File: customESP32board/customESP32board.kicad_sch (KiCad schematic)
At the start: 46 parts, among them J1 USB_B_Micro, J2 Conn_01x16_Pin, J3 Conn_01x16_Pin, Q1 S8050, Q2 S8050, Q3 BSS138, Q4 BSS138, Q5 BSS138, SW1 SW_Push, SW2 SW_Push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

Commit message: assigned footprint to all symbols
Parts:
- C1, C7: footprint (none) -> Capacitor_SMD:C_0805_2012Metric; link (none) -> https://makerselectronics.com/product/multilayer-ceramic-ca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
- C11: footprint (none) -> Capacitor_SMD:C_1206_3216Metric; link (none) -> https://uge-one.com/product/1206-solid-tantalum-smd-chip-ca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
- C3, C6: footprint (none) -> Capacitor_SMD:C_0603_1608Metric; link (none) -> https://makerselectronics.com/product/multilayer-ceramic-sm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
- D1: footprint Diode_THT:D_DO-41_SOD81_P10.16mm_Horizontal -> Diode_SMD:D_SMA_Handsoldering
- D11, D6, D7, D8: footprint (none) -> LED_THT:LED_D5.0mm-4_RGB
- D5, D9: footprint (none) -> LED_SMD:LED_0603_1608Metric
- J1: footprint (none) -> Connector_USB:USB_Micro-B_Wuerth_629105150521
- J2, J3: footprint (none) -> Connector_PinHeader_2.54mm:PinHeader_1x16_P2.54mm_Vertical; link (none) -> https://uge-one.com/product/pin-header-female-1x16-straight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
- R1, R11, R12, R16, R17, R18, R2, R3: footprint (none) -> Resistor_SMD:R_0805_2012Metric
- R10, R13, R14, R15, R4, R7, R8, R9: footprint (none) -> Resistor_SMD:R_0603_1608Metric
- R5, R6: footprint (none) -> Resistor_SMD:R_1206_3216Metric
- SW1: footprint (none) -> TS-1088-AR02016:SW_TS-1088-AR02016
- SW2: footprint (none) -> TS-1088-AR02016:SW_TS-1088-AR02016; link https://uge-one.com/product/smd-micro-push-button-switch-2p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 -> https://uge-one.com/product/smd-micro-switch-white-tact-s-3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
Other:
- title: customESP32S by Eng/Ahmed Adel -> customESP32board by Eng/Ahmed Adel
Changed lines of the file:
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@@
 	(paper "A4")
 	(title_block
-		(title "customESP32S by Eng/Ahmed Adel")
+		(title "customESP32board by Eng/Ahmed Adel")
 		(date "2025-09-23")
 		(rev "V1_1")
@@
 			)
 		)
-		(property "Footprint" ""
+		(property "Footprint" "Resistor_SMD:R_0603_1608Metric"
 			(at 140.97 120.142 90)
 			(effects
@@
 			)
 		)
-		(property "Footprint" ""
+		(property "Footprint" "LED_THT:LED_D5.0mm-4_RGB"
 			(at 201.93 90.17 0)
 			(effects
@@
 			)
 		)
-		(property "Footprint" ""
+		(property "Footprint" "Resistor_SMD:R_0805_2012Metric"
 			(at 190.5 141.478 90)
 			(effects
@@
 			)
 		)
-		(property "Footprint" ""
+		(property "Footprint" "Resistor_SMD:R_0603_1608Metric"
 			(at 147.32 64.008 90)
 			(effects
@@
 			)
 		)
-		(property "Footprint" ""
+		(property "Footprint" "Resistor_SMD:R_0805_2012Metric"
 			(at 145.542 127 90)
 			(effects
@@
 			)
 		)
-		(property "Footprint" ""
+		(property "Footprint" "Capacitor_SMD:C_1206_3216Metric"
 			(at 59.3852 95.25 0)
 			(effects
@@
 			)
 		)
-		(property "link" ""
+		(property "link" "https://uge-one.com/product/1206-solid-tantalum-smd-chip-capacitors-22uf-10v-type-a-3216/?srsltid=AfmBOopTQ543hj2REw3LW1Aad3g4Vye15Z8vCZf5dY69xXFxijASt_x6"
 			(at 58.42 91.44 0)
 			(effects
@@
 			)
 		)
-		(property "Footprint" ""
+		(property "Footprint" "Resistor_SMD:R_1206_3216Metric"
 			(at 107.188 38.1 90)
 			(effects
@@
 			)
 		)
-		(property "Footprint" ""
+		(property "Footprint" "Resistor_SMD:R_0805_2012Metric"
 			(at 190.5 151.638 90)
 			(effects
@@
 			)
 		)
-		(property "Footprint" ""
+		(property "Footprint" "Resistor_SMD:R_0805_2012Metric"
 			(at 145.542 165.1 90)
 			(effects
@@
 			)
 		)
-		(property "Footprint" ""
+		(property "Footprint" "Resistor_SMD:R_1206_3216Metric"
 			(at 93.218 38.1 90)
 			(effects
@@
 			)
 		)
-		(property "Footprint" ""
+		(property "Footprint" "Resistor_SMD:R_0805_2012Metric"
 			(at 87.63 151.638 90)
 			(effects
@@
 			)
 		)
-		(property "Footprint" ""
+		(property "Footprint" "Connector_USB:USB_Micro-B_Wuerth_629105150521"
 			(at 25.4 41.91 0)
 			(effects
@@
 			)
 		)
-		(property "Footprint" ""
+		(property "Footprint" "Connector_PinHeader_2.54mm:PinHeader_1x16_P2.54mm_Vertical"
 			(at 248.92 134.62 0)
 			(effects
@@
 			)
 		)
-		(property "Datasheet" "~"
+		(property "Datasheet" "https://uge-one.com/product/pin-header-female-1x16-straight-connector-2-54mm-pitch-blue/?srsltid=AfmBOoow7MnGPupESH2Bn80hXHz93AXS_C1RnlKSbnqCmVDw4ILT8D4U"
 			(at 248.92 134.62 0)
 			(effects
@@
 			)
 		)
-		(property "link" ""
+		(property "link" "https://uge-one.com/product/pin-header-female-1x16-straight-connector-2-54mm-pitch-blue/?srsltid=AfmBOoow7MnGPupESH2Bn80hXHz93AXS_C1RnlKSbnqCmVDw4ILT8D4U"
 			(at 248.92 134.62 0)
 			(effects
@@
 			)
 		)
-		(property "Footprint" "Diode_THT:D_DO-41_SOD81_P10.16mm_Horizontal"
+		(property "Footprint" "Diode_SMD:D_SMA_Handsoldering"
 			(at 52.07 31.115 0)
 			(effects
@@
 			)
 		)
-		(property "Footprint" ""
+		(property "Footprint" "TS-1088-AR02016:SW_TS-1088-AR02016"
 			(at 86.36 48.26 0)
 			(effects
@@
 			)
 		)
-		(property "Datasheet" "~"
+		(property "Datasheet" "https://uge-one.com/product/smd-micro-push-button-switch-2p-3x4x2mm/"
 			(at 86.36 48.26 0)
 			(effects
@@
 			)
 		)
-		(property "Footprint" ""
+		(property "Footprint" "Resistor_SMD:R_0805_2012Metric"
 			(at 87.63 177.038 90)
 			(effects
@@
 			)
 		)
-		(property "Footprint" ""
+		(property "Footprint" "Capacitor_SMD:C_0805_2012Metric"
 			(at 62.23 30.48 0)
 			(effects
@@
 			)
 		)
-		(property "link" ""
+		(property "link" "https://makerselectronics.com/product/multilayer-ceramic-capacitors-mlcc-smd-smt-10uf-%c2%b110-25v-0805/"
 			(at 62.23 30.48 0)
 			(effects
@@
 			)
 		)
-		(property "Footprint" ""
+		(property "Footprint" "Resistor_SMD:R_0603_1608Metric"
 			(at 190.5 131.318 90)
 			(effects
@@
 			)
 		)
-		(property "Footprint" ""
+		(property "Footprint" "Capacitor_SMD:C_0603_1608Metric"
 			(at 31.75 91.44 0)
 			(effects
@@
 			)
 		)
-		(property "link" ""
+		(property "link" "https://makerselectronics.com/product/multilayer-ceramic-smd-capacitor-mlcc-smd-smt-100nf-%c2%b110-50v-x7r-0603/"
 			(at 31.75 91.44 0)
 			(effects
@@
 			)
 		)
-		(property "Footprint" ""
+		(property "Footprint" "Capacitor_SMD:C_0805_2012Metric"
 			(at 20.32 91.44 0)
 			(effects
@@
 			)
 		)
-		(property "link" ""
+		(property "link" "https://makerselectronics.com/product/multilayer-ceramic-capacitors-mlcc-smd-smt-10uf-%c2%b110-25v-0805/"
 			(at 20.32 91.44 0)
 			(effects
@@
 			)
 		)
-		(property "Footprint" ""
+		(property "Footprint" "Connector_PinHeader_2.54mm:PinHeader_1x16_P2.54mm_Vertical"
 			(at 265.43 134.62 0)
 			(effects
@@
 			)
 		)
-		(property "Datasheet" "~"
+		(property "Datasheet" "https://uge-one.com/product/pin-header-female-1x16-straight-connector-2-54mm-pitch-blue/?srsltid=AfmBOoow7MnGPupESH2Bn80hXHz93AXS_C1RnlKSbnqCmVDw4ILT8D4U"
 			(at 265.43 134.62 0)
 			(effects
@@
 			)
 		)
-		(property "link" ""
+		(property "link" "https://uge-one.com/product/pin-header-female-1x16-straight-connector-2-54mm-pitch-blue/?srsltid=AfmBOoow7MnGPupESH2Bn80hXHz93AXS_C1RnlKSbnqCmVDw4ILT8D4U"
 			(at 265.43 134.62 0)
 			(effects
@@
 			)
 		)
-		(property "Footprint" ""
+		(property "Footprint" "Resistor_SMD:R_0603_1608Metric"
 			(at 147.32 42.418 90)
 			(effects
@@
 			)
 		)
-		(property "Footprint" ""
+		(property "Footprint" "Resistor_SMD:R_0603_1608Metric"
 			(at 140.97 141.732 90)
 			(effects
@@
 			)
 		)
-		(property "Footprint" ""
+		(property "Footprint" "TS-1088-AR02016:SW_TS-1088-AR02016"
 			(at 100.33 48.26 0)
 			(effects
@@
 			)
 		)
-		(property "Datasheet" "~"
+		(property "Datasheet" "https://uge-one.com/product/smd-micro-switch-white-tact-s-3-6-5-2-pin/"
 			(at 100.33 48.26 0)
 			(effects
@@
 			)
 		)
-		(property "link" "https://uge-one.com/product/smd-micro-push-button-switch-2p-3x4x2mm/"
+		(property "link" "https://uge-one.com/product/smd-micro-switch-white-tact-s-3-6-5-2-pin/"
 			(at 105.41 48.26 90)
 			(effects
@@
 			)
 		)
-		(property "Footprint" ""
+		(property "Footprint" "Capacitor_SMD:C_0603_1608Metric"
 			(at 105.41 185.42 0)
 			(effects
@@
 			)
 		)
-		(property "link" ""
+		(property "link" "https://makerselectronics.com/product/multilayer-ceramic-smd-capacitor-mlcc-smd-smt-100nf-%c2%b110-50v-x7r-0603/"
 			(at 105.41 185.42 90)
 			(effects
@@
 			)
 		)
-		(property "Footprint" ""
+		(property "Footprint" "Resistor_SMD:R_0805_2012Metric"
 			(at 91.948 81.28 90)
 			(effects
@@
 			)
 		)
-		(property "Footprint" ""
+		(property "Footprint" "Resistor_SMD:R_0603_1608Metric"
 			(at 140.97 159.512 90)
 			(effects
@@
 			)
 		)
-		(property "Footprint" ""
+		(property "Footprint" "LED_THT:LED_D5.0mm-4_RGB"
 			(at 207.01 140.97 0)
 			(effects
@@
 			)
 		)
-		(property "Footprint" ""
+		(property "Footprint" "Resistor_SMD:R_0603_1608Metric"
 			(at 147.32 53.848 90)
 			(effects
@@
 			)
 		)
-		(property "Footprint" ""
+		(property "Footprint" "LED_SMD:LED_0603_1608Metric"
 			(at 90.17 88.9 0)
 			(effects
@@
 			)
 		)
-		(property "Footprint" ""
+		(property "Footprint" "Resistor_SMD:R_0805_2012Metric"
 			(at 145.542 147.32 90)
 			(effects
@@
 			)
 		)
-		(property "Footprint" ""
+		(property "Footprint" "Resistor_SMD:R_0603_1608Metric"
 			(at 109.728 83.82 90)
 			(effects
@@
 			)
 		)
-		(property "Footprint" ""
+		(property "Footprint" "LED_SMD:LED_0603_1608Metric"
 			(at 107.95 91.44 0)
 			(effects
@@
 			)
 		)
-		(property "Footprint" ""
+		(property "Footprint" "LED_THT:LED_D5.0mm-4_RGB"
 			(at 201.93 67.31 0)
 			(effects
@@
 			)
 		)
-		(property "Footprint" ""
+		(property "Footprint" "LED_THT:LED_D5.0mm-4_RGB"
 			(at 201.93 43.18 0)
 			(effects

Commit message: generated BOM and created layout file
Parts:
- C11: value 22uF, 6.3v+ -> 22uF, 6.3v+, tantlum
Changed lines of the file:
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@@
 			)
 		)
-		(property "Value" "22uF, 6.3v+"
+		(property "Value" "22uF, 6.3v+, tantlum"
 			(at 53.34 93.726 0)
 			(effects

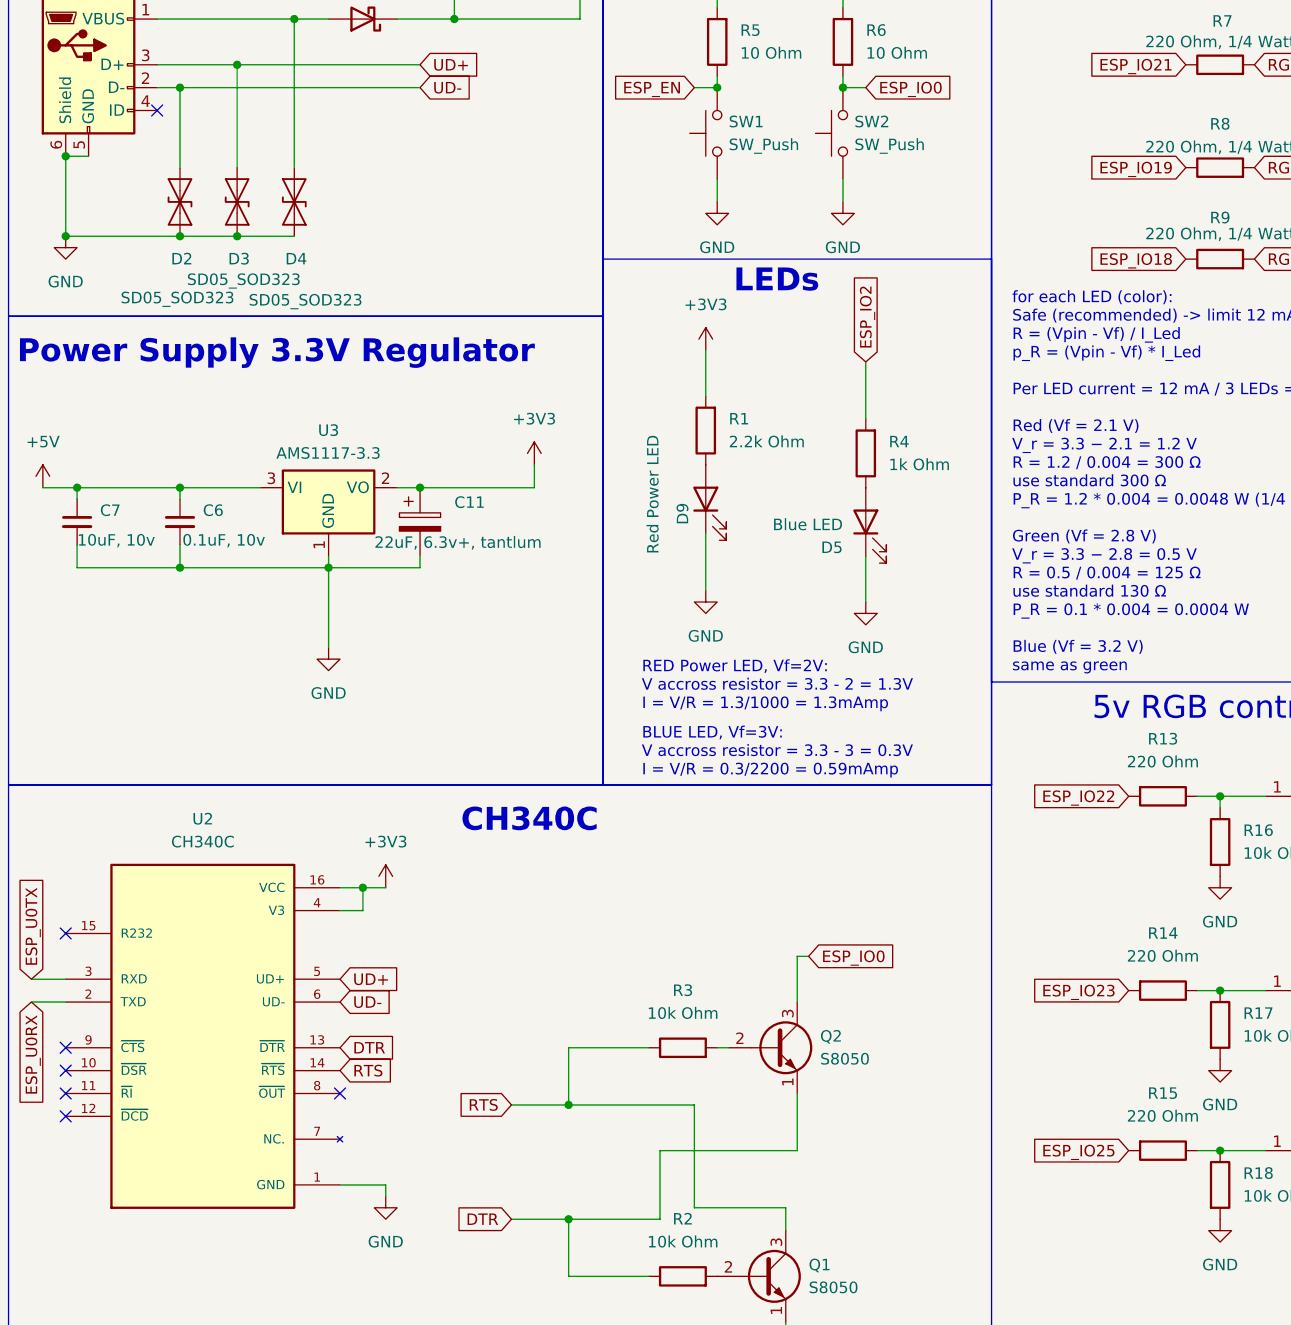
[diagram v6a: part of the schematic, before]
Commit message: continued layout, removed tvs diodes
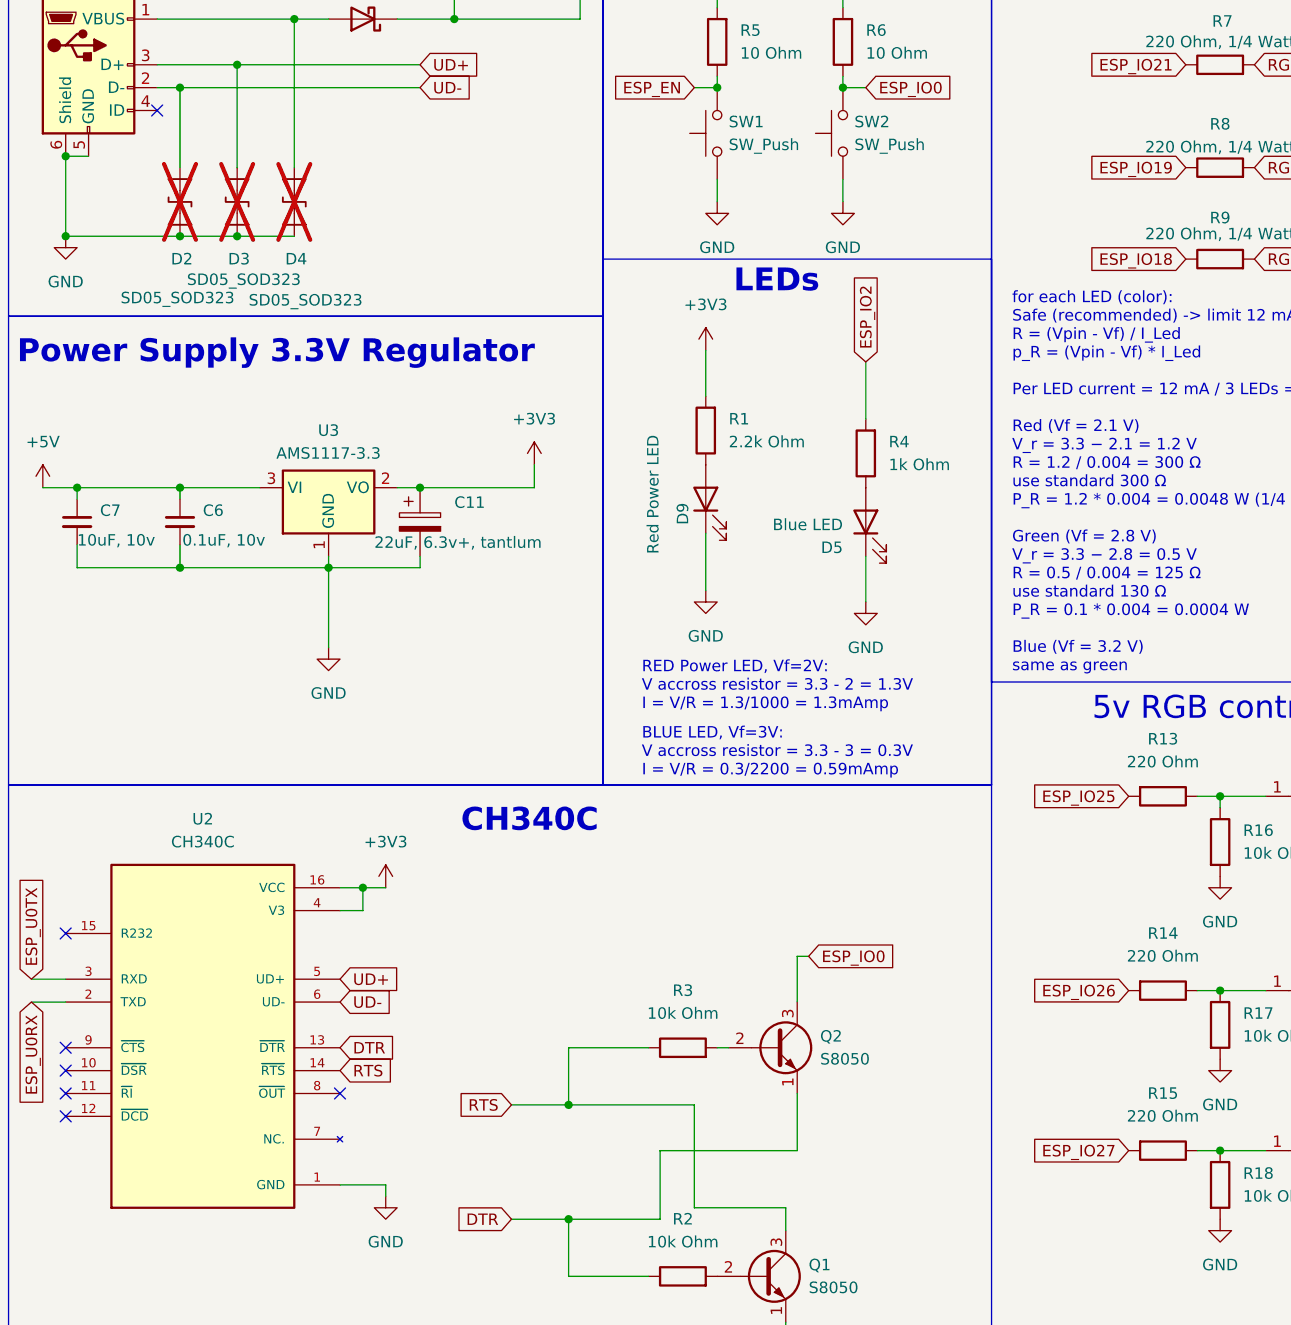
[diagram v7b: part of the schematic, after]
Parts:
- D2, D3, D4: now not fitted; now left out of the parts list
- Q1, Q2: footprint Package_TO_SOT_THT:TO-92_Inline -> Package_TO_SOT_SMD:SOT-23
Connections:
- net ESP_IO22: no longer R13.2
- net ESP_IO23: no longer R14.2
- net ESP_IO25: now also R13.2; no longer R15.2
- net ESP_IO26: now also R14.2
- net ESP_IO27: now also R15.2
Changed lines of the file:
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@@
 		)
 	)
-	(global_label "ESP_IO22"
+	(global_label "ESP_IO25"
 		(shape input)
 		(at 137.16 121.92 180)
@@
 		)
 	)
-	(global_label "ESP_IO23"
+	(global_label "ESP_IO26"
 		(shape input)
 		(at 137.16 143.51 180)
@@
 		)
 	)
-	(global_label "ESP_IO25"
+	(global_label "ESP_IO27"
 		(shape input)
 		(at 137.16 161.29 180)
@@
 			)
 		)
-		(property "Footprint" "Package_TO_SOT_THT:TO-92_Inline"
+		(property "Footprint" "Package_TO_SOT_SMD:SOT-23"
 			(at 102.87 151.765 0)
 			(effects
@@
 		(unit 1)
 		(exclude_from_sim no)
-		(in_bom yes)
-		(on_board yes)
-		(dnp no)
+		(in_bom no)
+		(on_board no)
+		(dnp yes)
 		(property "Reference" "D4"
 			(at 43.434 62.23 90)
@@
 		(unit 1)
 		(exclude_from_sim no)
-		(in_bom yes)
-		(on_board yes)
-		(dnp no)
+		(in_bom no)
+		(on_board no)
+		(dnp yes)
 		(property "Reference" "D3"
 			(at 37.084 62.23 90)
@@
 			)
 		)
-		(property "Footprint" "Package_TO_SOT_THT:TO-92_Inline"
+		(property "Footprint" "Package_TO_SOT_SMD:SOT-23"
 			(at 101.6 177.165 0)
 			(effects
@@
 		(unit 1)
 		(exclude_from_sim no)
-		(in_bom yes)
-		(on_board yes)
-		(dnp no)
+		(in_bom no)
+		(on_board no)
+		(dnp yes)
 		(property "Reference" "D2"
 			(at 30.734 62.23 90)

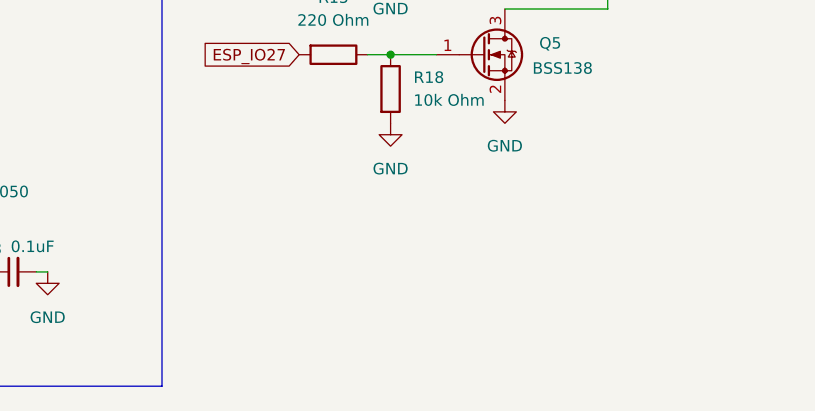
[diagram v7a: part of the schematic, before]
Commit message: adjusted placement to 0.1 mm grid
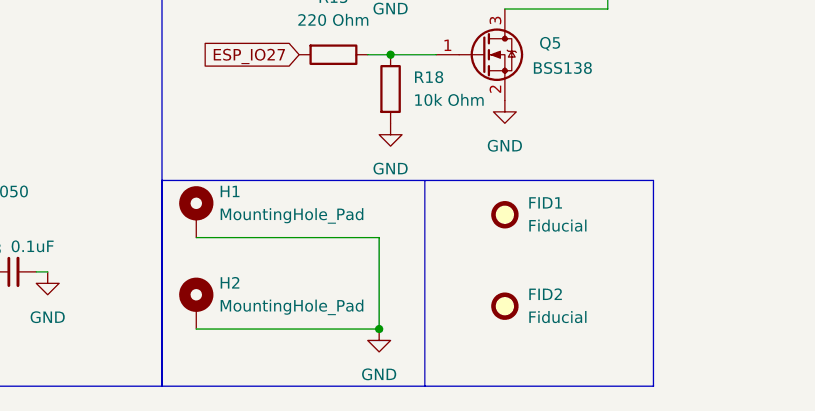
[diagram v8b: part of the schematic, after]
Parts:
- added FID1, FID2: Fiducial, Fiducial:Fiducial_0.5mm_Mask1.5mm, symbol Mechanical:Fiducial
- added H1, H2: MountingHole_Pad, MountingHole:MountingHole_2.2mm_M2_Pad_Via, symbol Mechanical:MountingHole_Pad
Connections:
- net GND: now also H1.1, H2.1
